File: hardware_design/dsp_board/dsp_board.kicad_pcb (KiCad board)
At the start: 2 copper layers, 60.8 x 42.5 mm, 73 parts, among them J1 USB4800-03-A_REVA, J2 SM06B-SRSS-TB(LF)(SN), J3 RCJ-041, J4 RCJ-041, J5 RCJ-041, J6 RCJ-041, J7 RCJ-041, J8 RCJ-041, Q2 BC807, U1 TPD2S017DBVR, U2 AP2112K-3.3TRG1, U3 AP2112K-3.3TRG1, U4 24LC128-E/MS, U5 ESP32-S3-WROOM-1-N16R2, U6 ADAU1701JSTZ, Y1 ECS-122.8-20-3X-EN-TR

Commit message: Queues
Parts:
- J2: moved to B.Cu
- moved C31 115.1 mm to (37.0, 104.5), turned to -90 degrees
- moved C32 105.5 mm to (44.2, 104.5), turned to -90 degrees
- moved C35 96.0 mm to (51.5, 104.5), turned to -90 degrees
- moved R14 92.3 mm to (39.2, 124.8), turned to -135 degrees
- moved C36 91.8 mm to (58.8, 104.5), turned to -90 degrees
- moved R12 90.1 mm to (46.5, 131.2), turned to -90 degrees
- moved C29 88.5 mm to (46.5, 134.8), turned to -90 degrees
- moved C30 77.9 mm to (61.5, 134.8), turned to -90 degrees
- moved R13 75.7 mm to (61.5, 131.2), turned to -90 degrees
- moved R7 48.8 mm to (86.5, 105.2), turned to -90 degrees
- moved J2 21.7 mm to (82.8, 117.0), turned to -90 degrees
- moved J3 15.0 mm to (40.0, 140.0)
- moved J4 15.0 mm to (55.0, 140.0)
- moved C4 7.07 mm to (70.7, 131.2)
- moved U2 7.02 mm to (67.0, 130.5)
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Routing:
- net VBUS: track 0.00 -> 43.3 mm
- net +3.3V: track 0.00 -> 42.9 mm, vias 0 -> 2
- net USB_DN: track 0.00 -> 36.7 mm
- net USB_DP: track 0.00 -> 35.8 mm
- net Net-(C1-Pad1): track 0.00 -> 17.6 mm
- net BOOT: track 0.00 -> 15.4 mm, vias 0 -> 1
- net UART0_RX: track 0.00 -> 13.9 mm, vias 0 -> 1
- net EN: track 0.00 -> 13.8 mm, vias 0 -> 1
- net UART0_TX: track 0.00 -> 12.4 mm, vias 0 -> 1
- net Net-(C30-Pad2): track 0.00 -> 8.14 mm
- net Net-(C29-Pad2): track 0.00 -> 8.14 mm
- net Net-(J1-DN1): track 0.00 -> 7.69 mm
- net Net-(J1-CC1): track 0.00 -> 5.89 mm
- net Net-(J1-DP1): track 0.00 -> 5.41 mm
- net Net-(J1-CC2): track 0.00 -> 3.66 mm
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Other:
- board size 60.8 x 42.5 mm -> 60.8 x 53.2 mm

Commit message: Improved PCB
Improved main PCB design
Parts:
- C8, R14, R7, R8, U4: moved to B.Cu
- moved R15 99.0 mm to (45.0, 124.8), turned to 180 degrees
- moved C33 97.7 mm to (45.0, 127.8), turned to 180 degrees
- moved C4 86.7 mm to (157.2, 137.2)
- moved C5 86.7 mm to (157.2, 135.8)
- moved U2 86.7 mm to (153.5, 136.5)
- moved R17 83.6 mm to (60.0, 124.8), turned to 180 degrees
- moved C37 81.7 mm to (60.0, 127.8), turned to 180 degrees
- moved R16 73.6 mm to (74.2, 124.8), turned to 180 degrees
- moved C34 69.3 mm to (74.2, 127.8), turned to 180 degrees
- moved R18 59.1 mm to (89.2, 124.8), turned to 180 degrees
- moved C38 53.4 mm to (89.2, 127.8), turned to 180 degrees
- moved J3 52.2 mm to (55.0, 90.0), turned to 90 degrees
- moved J4 52.2 mm to (40.0, 90.0), turned to 90 degrees
- moved J6 52.2 mm to (70.0, 140.0), turned to -90 degrees
- moved J7 52.2 mm to (55.0, 140.0), turned to -90 degrees
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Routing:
- net USB_DN: track 36.7 -> 0.00 mm
- net USB_DP: track 35.8 -> 0.00 mm
- net VBUS: track 43.3 -> 17.4 mm
- net +3.3V: track 42.9 -> 28.1 mm
- net Net-(C30-Pad2): track 8.14 -> 0.00 mm
- net Net-(C29-Pad2): track 8.14 -> 0.00 mm
- net EN: track 13.8 -> 17.6 mm
- net BOOT: track 15.4 -> 18.4 mm
- net Net-(C30-Pad1): track 1.96 -> 0.00 mm
- net Net-(C29-Pad1): track 1.96 -> 0.00 mm
- net adcRes: track 0.00 -> 0.99 mm, vias 0 -> 1
- net UART0_TX: track 12.4 -> 13.1 mm
- net Net-(C1-Pad1): track 17.6 -> 17.1 mm
- net Net-(J1-CC2): track 3.66 -> 3.16 mm
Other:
- board size 60.8 x 53.2 mm -> 57 x 53 mm

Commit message: Mainboard progress
Layout progress on prototype mainboard
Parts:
- C10, C13, C14, C15, C16, C17, C18, C19, C20, C21, C22, C23, C24, C25, C26, C27, C28, C9, R11: moved to B.Cu
- moved R10 95.2 mm to (37.0, 117.2)
- moved Y1 94.5 mm to (39.0, 120.5)
- moved C14 94.2 mm to (35.8, 107.2), turned to 180 degrees
- moved C21 88.6 mm to (36.2, 125.2), turned to 90 degrees
- moved C13 87.8 mm to (35.8, 109.0), turned to 180 degrees
- moved C25 86.7 mm to (44.0, 114.2), turned to 180 degrees
- moved R11 85.8 mm to (44.0, 110.8), turned to 180 degrees
- moved C26 85.0 mm to (44.0, 112.5), turned to 180 degrees
- moved C28 84.9 mm to (51.5, 121.2)
- moved C24 84.1 mm to (51.8, 116.0)
- moved C16 83.5 mm to (48.2, 121.2)
- moved C22 82.5 mm to (41.8, 125.2), turned to 90 degrees
- moved C23 81.0 mm to (51.8, 114.2)
- moved C27 80.1 mm to (51.5, 119.5)
- moved C15 79.4 mm to (48.3, 119.5)
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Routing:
- net adc1: track 0.00 -> 19.7 mm
- net +3.3VA: track 0.00 -> 13.5 mm
- net USB_DP: track 0.00 -> 12.8 mm
- net USB_DN: track 0.00 -> 12.6 mm
- net adc2: track 0.00 -> 12.4 mm
- net MCLKI: track 0.00 -> 10.2 mm, vias 0 -> 1
- net Net-(C21-Pad2): track 0.00 -> 7.51 mm, vias 0 -> 1
- net FILTA: track 0.00 -> 4.57 mm, vias 0 -> 1
- net OSCO: track 0.00 -> 4.27 mm
- net adcRes: track 0.99 -> 4.02 mm
- net VBUS: track 17.4 -> 15.2 mm
- net PLL_LF: track 0.00 -> 1.90 mm, vias 0 -> 1
- net FILTD: track 0.00 -> 1.78 mm
- net EN: track 17.6 -> 18.4 mm

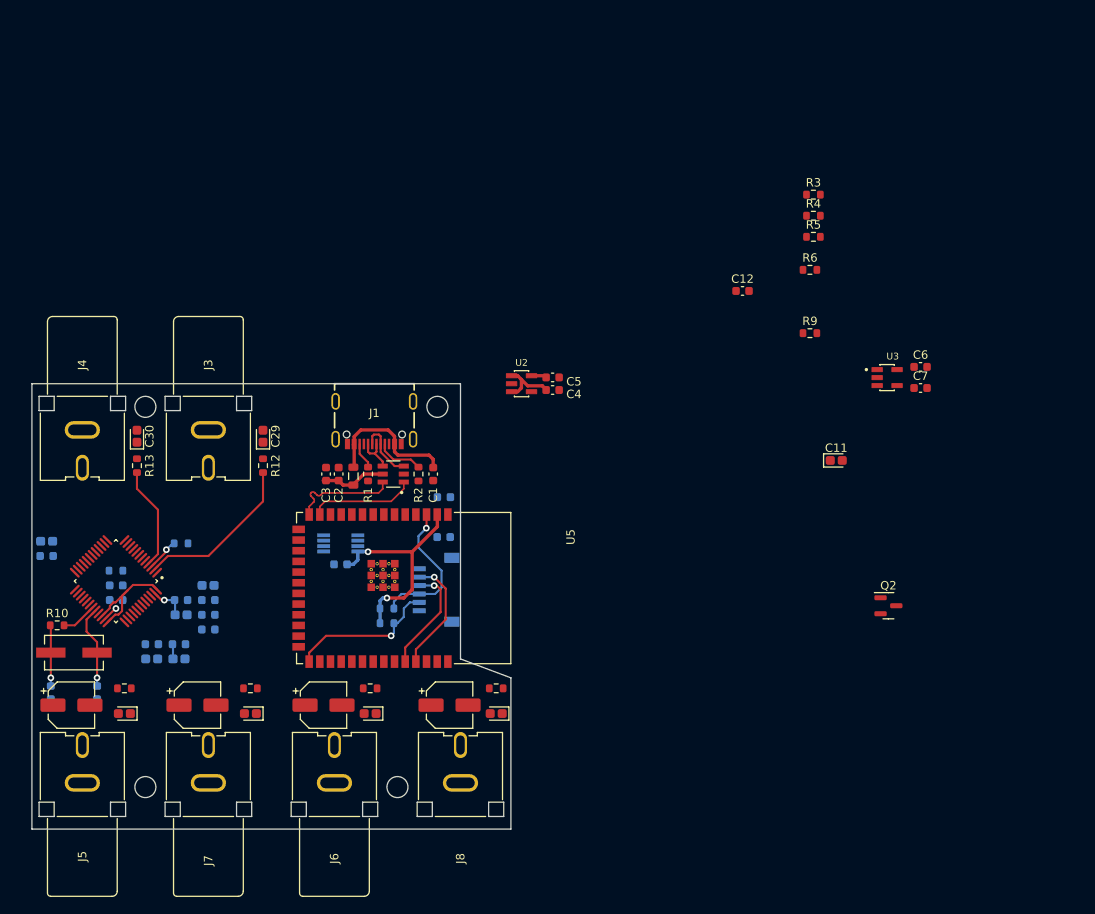
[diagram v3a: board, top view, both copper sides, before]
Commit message: PCB layout complete
PCB layout and routing complete.
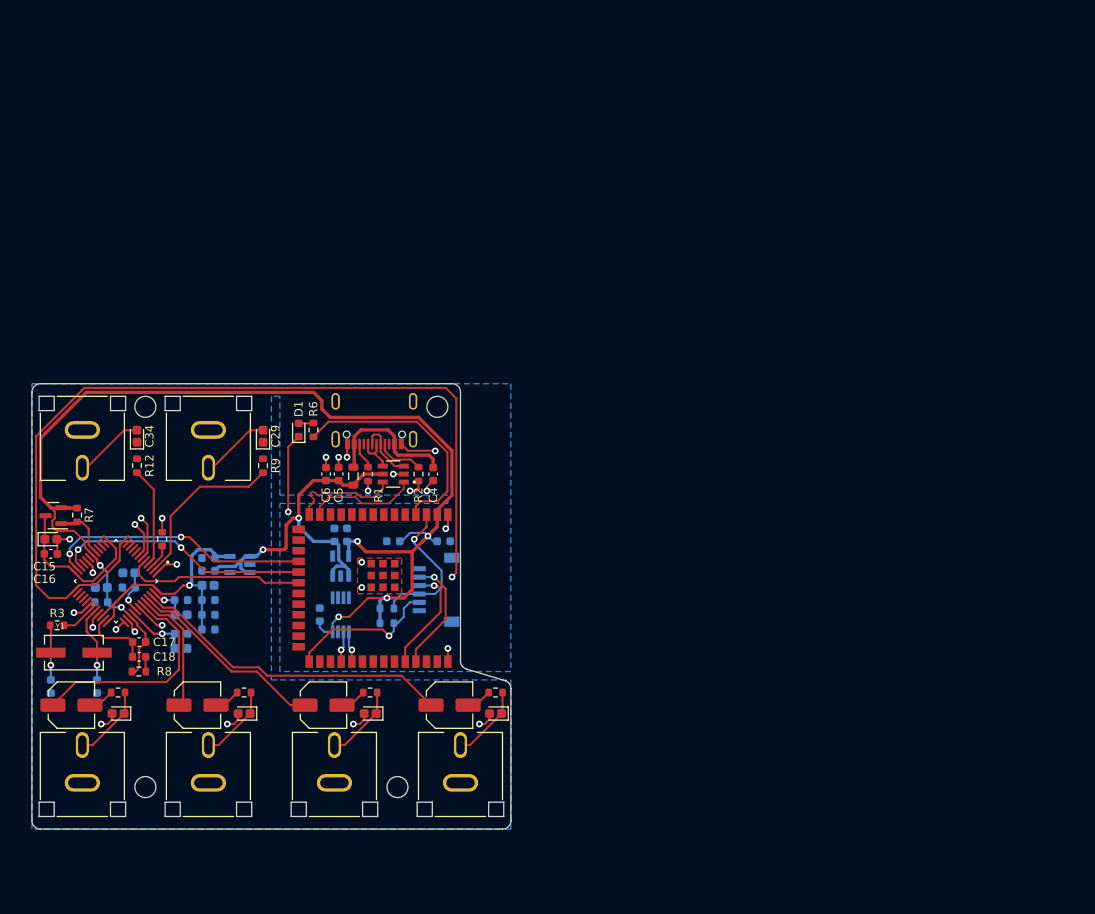
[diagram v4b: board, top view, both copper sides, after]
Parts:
- removed the R3 at (127.0, 66.0)
- removed the R4 at (127.0, 68.5)
- removed the R5 at (127.0, 71.0)
- added D1: LED, Diode_SMD:D_0603_1608Metric, F.Cu at (65.8, 94.0)
- C17: renamed from C25; moved to F.Cu
- C18: renamed from C26; moved to F.Cu
- C2: renamed from C5; moved to B.Cu
- C3: renamed from C6; moved to B.Cu
- C7: renamed from C4; moved to B.Cu
- C8: renamed from C7; moved to B.Cu
- R14: moved to F.Cu
- R6: value 2k20 -> 1k
- R8: renamed from R11; moved to F.Cu
- U2, U3: moved to B.Cu
- moved Q1 99.9 mm to (36.6, 104.2), turned to 180 degrees
- moved C15 93.9 mm to (36.2, 107.0)
- moved R7 89.9 mm to (39.4, 104.1), turned to -90 degrees
- moved C16 88.1 mm to (36.2, 108.8), turned to 180 degrees
- moved C3 87.8 mm to (55.0, 109.2), turned to 180 degrees
- moved C8 87.5 mm to (55.0, 110.8), turned to 180 degrees
- moved U3 80.2 mm to (58.8, 110.0), turned to 180 degrees
- moved R6 62.1 mm to (67.5, 94.0), turned to 90 degrees
- moved R15 45.0 mm to (44.2, 125.2)
- moved C30 45.0 mm to (83.7, 126.8)
- moved C36 45.0 mm to (38.7, 126.8)
- moved C38 45.0 mm to (44.2, 127.8)
- moved J4 45.0 mm to (85.0, 140.0)
- moved J8 45.0 mm to (40.0, 140.0)
- moved R10 44.2 mm to (89.2, 125.2)
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- renumbered C8 to C1, C9 to C10, C10 to C11, C22 to C12, C23 to C13, C24 to C14, C11 to C15, C12 to C16, C15 to C19, C27 to C20, C28 to C21, C16 to C22, C13 to C23, C14 to C24, C17 to C25, C18 to C26, C19 to C27, C20 to C28, C31 to C30, C32 to C31, C33 to C32, C34 to C33, C30 to C34, C1 to C4, C2 to C5, C3 to C6, C21 to C9, J5 to J4, J6 to J5, J4 to J6, Q2 to Q1, R15 to R10, R16 to R11, R13 to R12, R17 to R13, R18 to R15, R10 to R3, R7 to R4, R8 to R5, R9 to R7, R12 to R9, U6 to U5, U5 to U6
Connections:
- R6 pad 1: +3.3V -> Net-(U6-IO4)
- R6 pad 2: I2C1_SDA -> Net-(D1-A)
- U6 pad 18: unconnected-(U5-IO10-Pad18) -> I2C0_SCL
- U6 pad 19: unconnected-(U5-IO11-Pad19) -> I2C0_SDA
- U6 pad 20: I2C0_SCL -> ADA_reset
- U6 pad 21: I2C0_SDA -> unconnected-(U6-IO13-Pad21)
- U6 pad 22: I2C1_SCL -> unconnected-(U6-IO14-Pad22)
- U6 pad 30: unconnected-(U5-IO37-Pad30) -> I2C1_SCL
- U6 pad 31: unconnected-(U5-IO38-Pad31) -> I2C1_SDA
- U6 pad 4: unconnected-(U5-IO4-Pad4) -> Net-(U6-IO4)
- U6 pad 8: I2C1_SDA -> unconnected-(U6-IO15-Pad8)
- U6 pad 9: ADA_reset -> unconnected-(U6-IO16-Pad9)
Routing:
- net GND1: track 0.00 -> 164.1 mm, vias 0 -> 28
- net +3.3V: track 28.1 -> 147.3 mm, vias 2 -> 6
- net vout0: track 0.00 -> 38.7 mm
- net I2C0_SCL: track 0.00 -> 31.9 mm, vias 0 -> 2
- net I2C0_SDA: track 0.00 -> 30.5 mm, vias 0 -> 2
- net VBUS: track 15.2 -> 44.1 mm, vias 0 -> 2
- net Net-(U6-IO4): track 0.00 -> 28.3 mm
- net vout3: track 0.00 -> 27.0 mm
- net vout1: track 0.00 -> 23.9 mm
- net ADA_reset: track 0.00 -> 22.0 mm
- net +3.3VA: track 13.5 -> 33.7 mm, vias 0 -> 1
- net Net-(Q1-C): track 0.00 -> 18.7 mm
- net vout2: track 0.00 -> 15.1 mm
- net GND: track 0.00 -> 9.48 mm, vias 0 -> 1
- net Net-(C37-Pad1): track 0.00 -> 9.06 mm
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- added copper zone on B.Cu, net GND1
- added copper zone on F.Cu, net GND1
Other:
- outline, holes or cut-outs redrawn
- board text added: "OUT 1"
- board text added: "OUT 2"
- board text added: "OUT 3"
- board text added: "OUT 4"

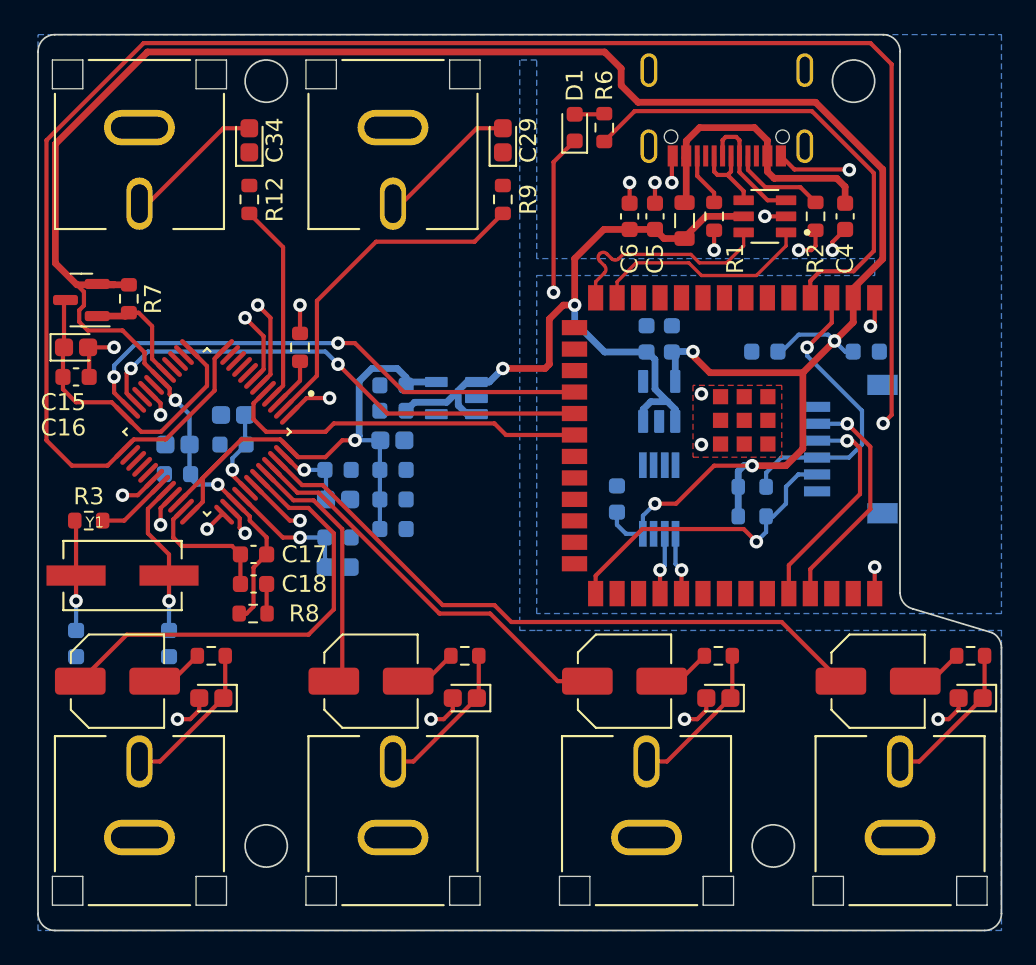
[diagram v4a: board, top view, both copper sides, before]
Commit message: Silkscreen improvements
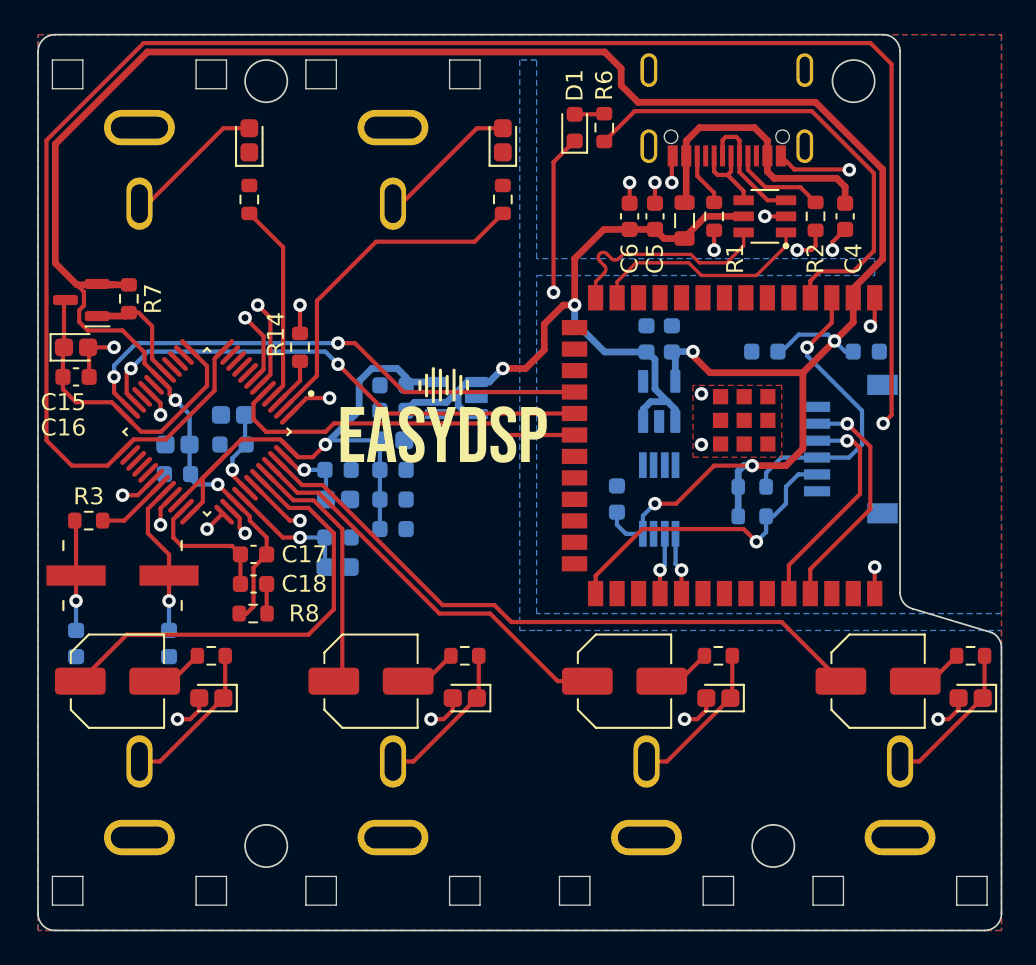
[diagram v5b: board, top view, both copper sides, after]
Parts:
- added REF**: EasyDSP logo, Library:EasyDSP logo, F.Cu at (58.0, 111.0)
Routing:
- net +3.3VA: track 33.7 -> 34.6 mm
- net VBUS: track 44.1 -> 43.4 mm
- added copper zone on F.Cu, net (none)
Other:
- board text added: "IN 1"
- board text added: "IN 2"
- board text added: "Prototype board v0.1"
